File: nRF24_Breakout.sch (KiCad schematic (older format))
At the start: 2 parts, among them J1 Conn_01x08_Male, U1 nRF24

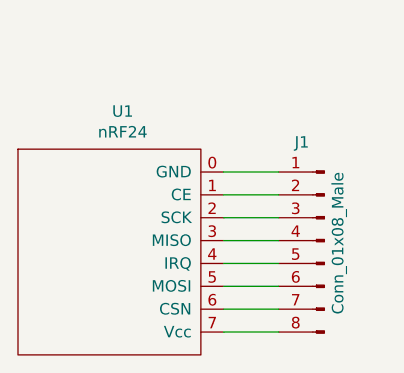
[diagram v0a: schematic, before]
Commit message: Updated Connector Pins
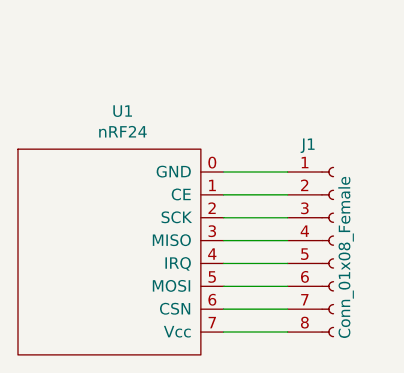
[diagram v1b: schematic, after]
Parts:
- removed J1: Conn_01x08_Male, Connector_PinHeader_2.00mm:PinHeader_1x08_P2.00mm_Vertical, symbol Connector:Conn_01x08_Male
- added J1: Conn_01x08_Female, Connector_PinHeader_2.54mm:PinHeader_1x08_P2.54mm_Vertical, symbol Connector:Conn_01x08_Female
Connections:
- net at U1.0 (GND): now also J1.1 (Pin_1)
- net at U1.1 (CE): now also J1.2 (Pin_2)
- net at U1.2 (SCK): now also J1.3 (Pin_3)
- net at U1.3 (MISO): now also J1.4 (Pin_4)
- net at U1.4 (IRQ): now also J1.5 (Pin_5)
- net at U1.5 (MOSI): now also J1.6 (Pin_6)
- net at U1.6 (CSN): now also J1.7 (Pin_7)
- net at U1.7 (Vcc): now also J1.8 (Pin_8)
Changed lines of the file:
@@
 $EndDescr
-$Comp
-L Connector:Conn_01x08_Male J1
-U 1 1 616E2C07
-P 6540 3760
-F 0 "J1" H 6670 4190 50  0000 R CNN
-F 1 "Conn_01x08_Male" V 6480 4060 50  0000 R CNN
-F 2 "Connector_PinHeader_2.00mm:PinHeader_1x08_P2.00mm_Vertical" H 6540 3760 50  0001 C CNN
-F 3 "~" H 6540 3760 50  0001 C CNN
-	1    6540 3760
-	-1   0    0    -1
-$EndComp
 $Comp
 L My_KiCad_Symbol_Library:nRF24 U1
@@
 	1    0    0    -1
 $EndComp
+$Comp
+L Connector:Conn_01x08_Female J1
+U 1 1 617389BA
+P 6580 3760
+F 0 "J1" H 6440 4180 50  0000 L CNN
+F 1 "Conn_01x08_Female" V 6630 3330 50  0000 L CNN
+F 2 "Connector_PinHeader_2.54mm:PinHeader_1x08_P2.54mm_Vertical" H 6580 3760 50  0001 C CNN
+F 3 "~" H 6580 3760 50  0001 C CNN
+	1    6580 3760
+	1    0    0    -1
+$EndComp
 Wire Wire Line
-	6100 3460 6340 3460
+	6100 3460 6380 3460
 Wire Wire Line
-	6100 3560 6340 3560
+	6100 3560 6380 3560
 Wire Wire Line
-	6340 3660 6100 3660
+	6100 3660 6380 3660
 Wire Wire Line
-	6100 3760 6340 3760
+	6100 3760 6380 3760
 Wire Wire Line
-	6340 3860 6100 3860
+	6100 3860 6380 3860
 Wire Wire Line
-	6100 3960 6340 3960
+	6100 3960 6380 3960
 Wire Wire Line
-	6340 4060 6100 4060
+	6100 4060 6380 4060
 Wire Wire Line
-	6100 4160 6340 4160
+	6100 4160 6380 4160
 $EndSCHEMATC

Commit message: Added filtering cap
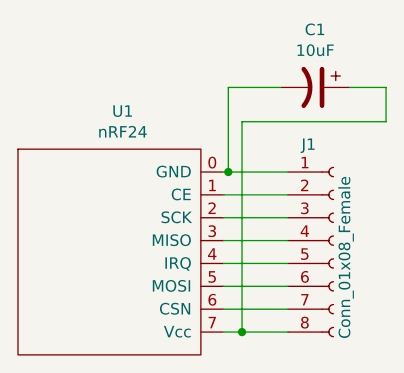
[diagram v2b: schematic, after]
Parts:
- added C1: 10uF, Capacitor_THT:CP_Radial_D10.0mm_P5.00mm, symbol Device:CP1
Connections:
- net at J1.1 (Pin_1), U1.0 (GND): now also C1.2
- net at J1.8 (Pin_8), U1.7 (Vcc): now also C1.1
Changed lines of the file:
@@
 $EndComp
 Wire Wire Line
-	6100 3460 6380 3460
+	6100 3460 6120 3460
 Wire Wire Line
 	6100 3560 6380 3560
@@
 	6100 4060 6380 4060
 Wire Wire Line
-	6100 4160 6380 4160
+	6100 4160 6180 4160
+$Comp
+L Device:CP1 C1
+U 1 1 6174D65A
+P 6500 3090
+F 0 "C1" V 6248 3090 50  0000 C CNN
+F 1 "10uF" V 6339 3090 50  0000 C CNN
+F 2 "Capacitor_THT:CP_Radial_D10.0mm_P5.00mm" H 6500 3090 50  0001 C CNN
+F 3 "~" H 6500 3090 50  0001 C CNN
+	1    6500 3090
+	0    1    1    0
+$EndComp
+Wire Wire Line
+	6350 3090 6120 3090
+Wire Wire Line
+	6120 3090 6120 3460
+Connection ~ 6120 3460
+Wire Wire Line
+	6120 3460 6380 3460
+Wire Wire Line
+	6810 3090 6810 3240
+Wire Wire Line
+	6810 3240 6180 3240
+Wire Wire Line
+	6180 3240 6180 4160
+Connection ~ 6180 4160
+Wire Wire Line
+	6180 4160 6380 4160
+Wire Wire Line
+	6650 3090 6810 3090
 $EndSCHEMATC
